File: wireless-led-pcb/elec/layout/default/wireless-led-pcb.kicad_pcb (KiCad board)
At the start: 2 copper layers, 225.7 x 100.8 mm, 0 parts

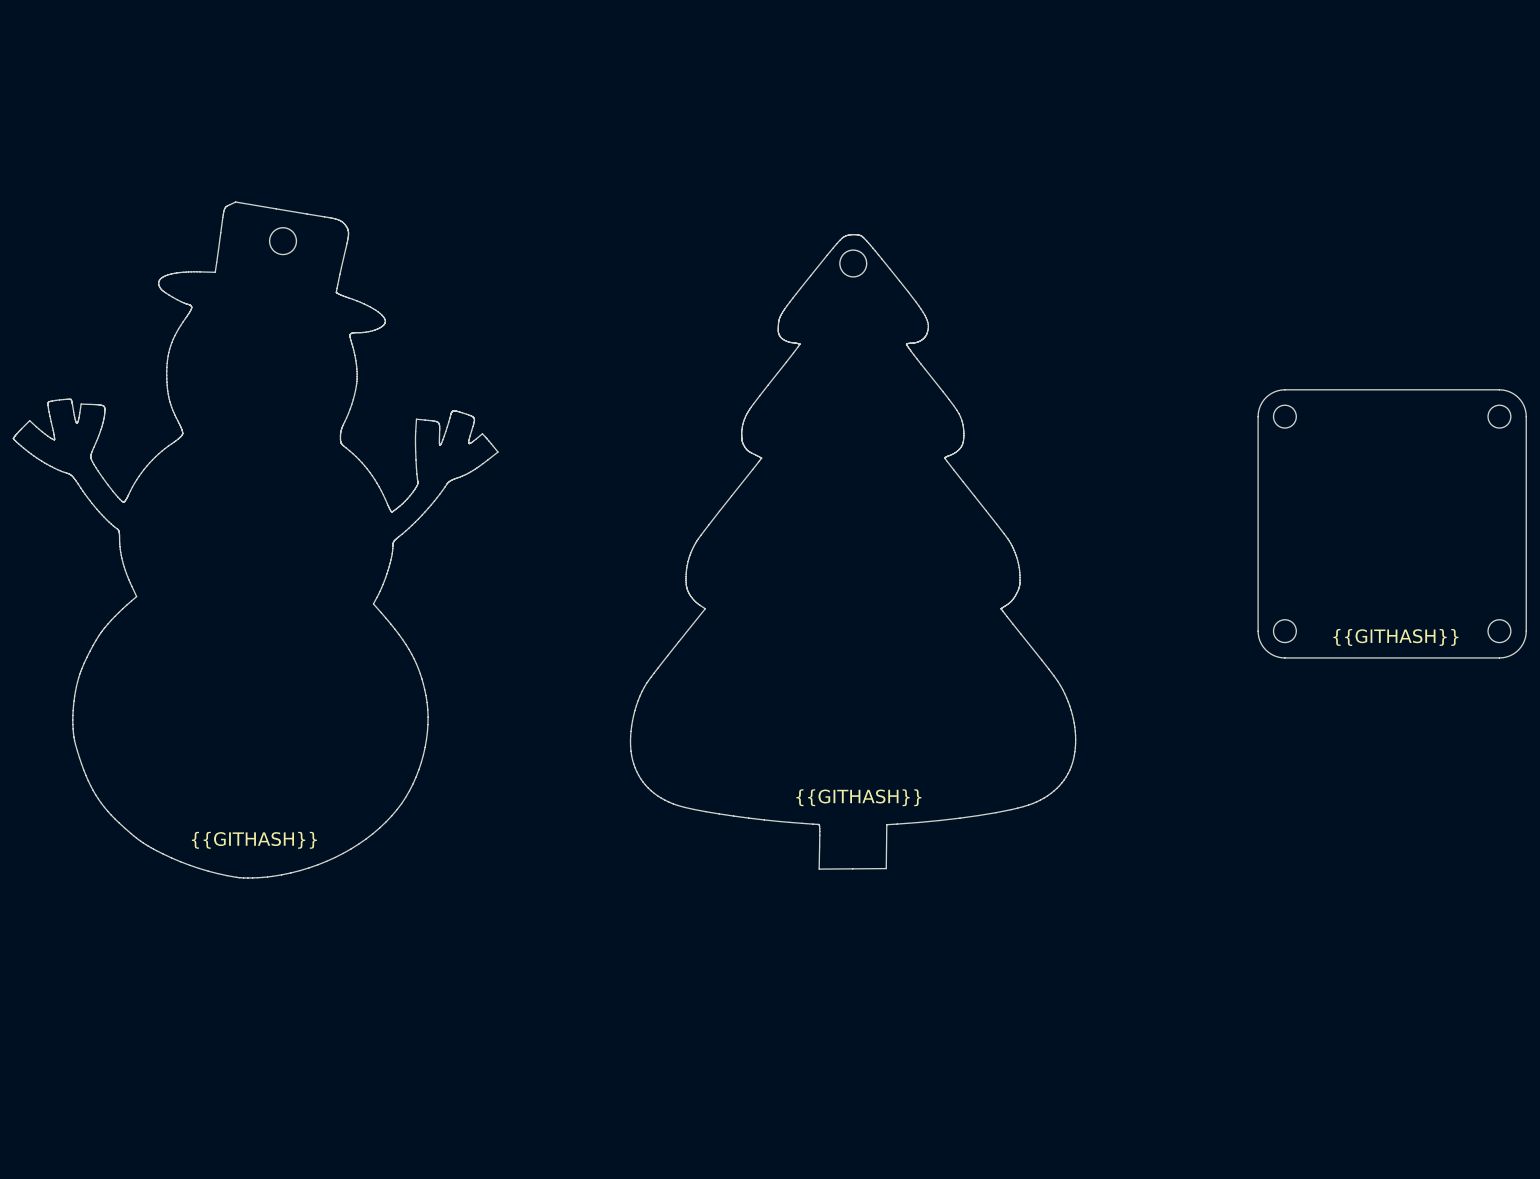
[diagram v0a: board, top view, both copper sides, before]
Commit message: Just started basic component organization in the layout. 1% done.
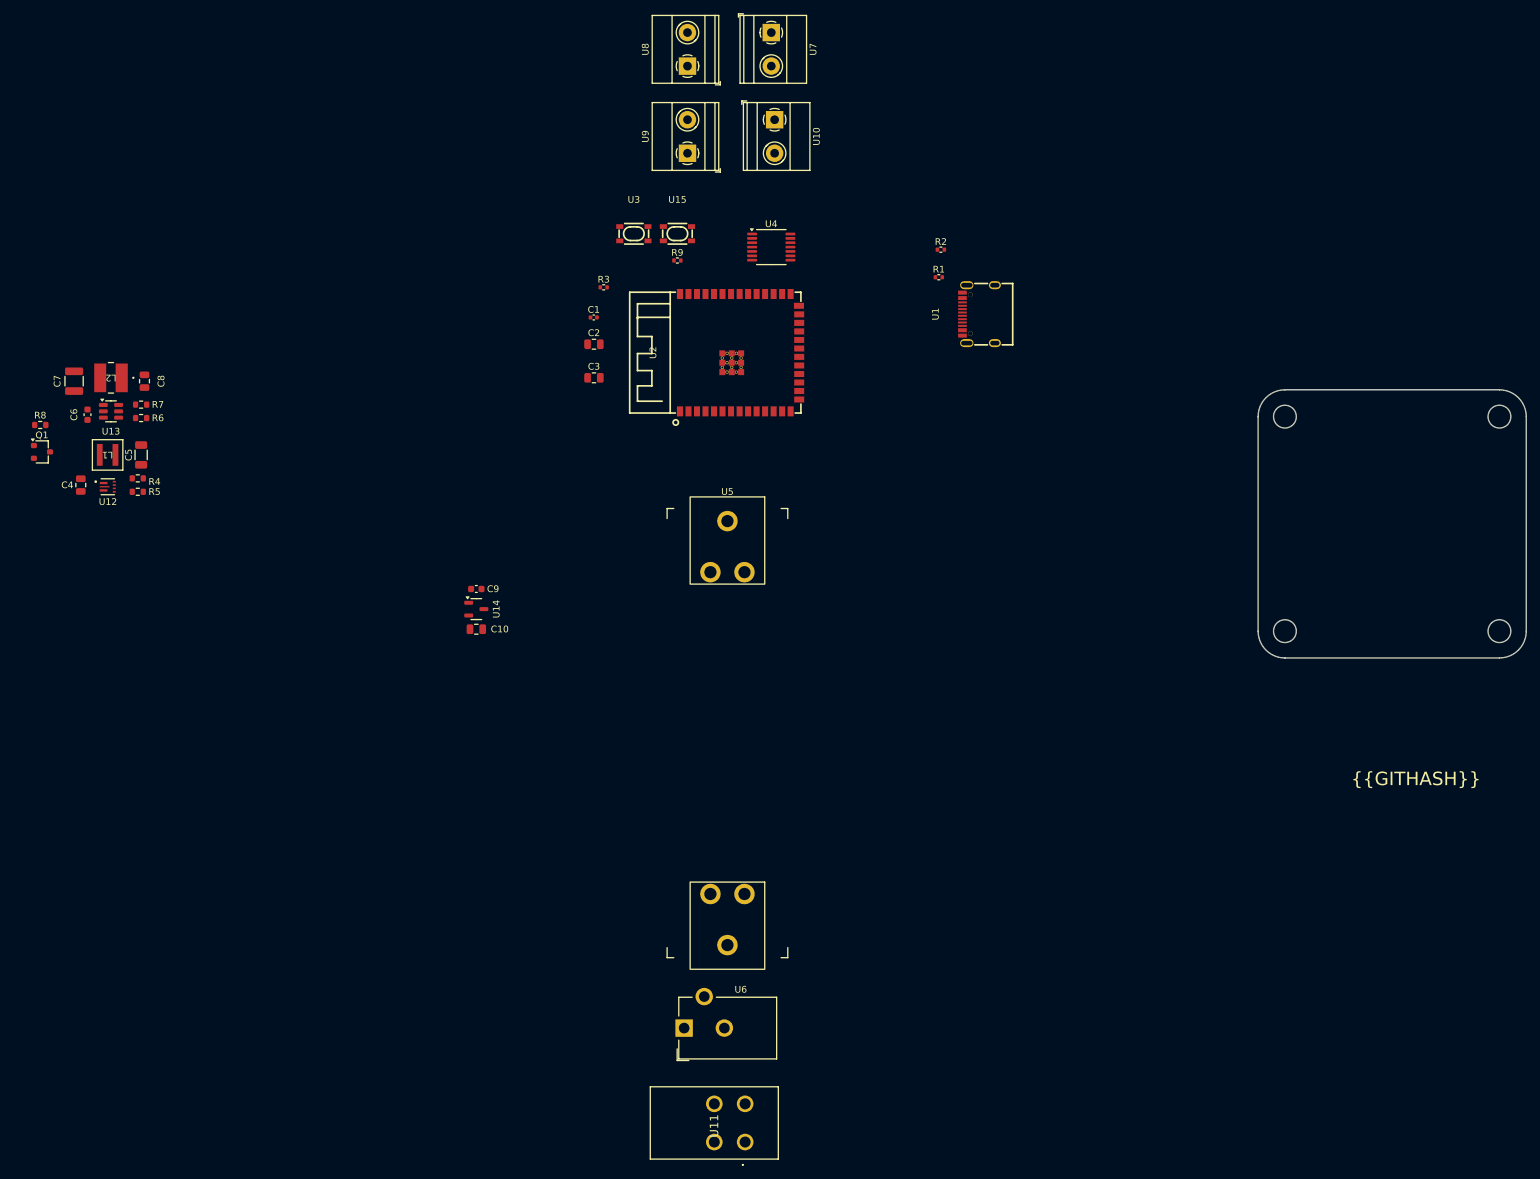
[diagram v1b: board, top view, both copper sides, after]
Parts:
- added C1: 16V 100nF X7R ±10% 0402 Multilayer Ceramic Capacitors MLCC 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, lib:C0402, F.Cu at (122.5, 67.0)
- added C10: 25V 10uF X5R ±10% 0805 Multilayer Ceramic Capacitors MLCC -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, lib:C0805, F.Cu at (105.0, 113.5)
- added C2: 25V 10uF X5R ±10% 0805 Multilayer Ceramic Capacitors MLCC -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, lib:C0805, F.Cu at (122.5, 71.0)
- added C3: 25V 10uF X5R ±10% 0805 Multilayer Ceramic Capacitors MLCC -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, lib:C0805, F.Cu at (122.5, 76.0)
- added C4: 25V 10uF X5R ±10% 0805 Multilayer Ceramic Capacitors MLCC -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, lib:C0805, F.Cu at (46.0, 92.0)
- added C5: 10V 47uF X5R ±20% 1206 Multilayer Ceramic Capacitors MLCC -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, lib:C1206, F.Cu at (55.0, 87.5)
- added C6: 10V 3.3uF X5R ±10% 0603 Multilayer Ceramic Capacitors MLCC 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, lib:C0603, F.Cu at (47.0, 81.5)
- added C7: 16V 47uF X7R ±10% 1210 Multilayer Ceramic Capacitors MLCC -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, lib:C1210, F.Cu at (45.0, 76.5)
- added C8: 50V 100nF X7R ±10% 0805 Multilayer Ceramic Capacitors MLCC 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, lib:C0805, F.Cu at (55.5, 76.5)
- added C9: 50V 1uF X5R ±10% 0603 Multilayer Ceramic Capacitors MLCC - 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, lib:C0603, F.Cu at (105.0, 107.5)
- added L1: 1uH +/- 20%, lib:IND_XAL4020_COC, F.Cu at (50.0, 87.5)
- added L2: 6.8uH +/- 20%, lib:IND_8357068_WRE, F.Cu at (50.5, 76.0)
- added Q1: , Package_TO_SOT_SMD:SC-59, F.Cu at (40.2, 87.0)
- added R1: 62.5mW Thick Film Resistors 50V ±100ppm/℃ ±1% 4.7kΩ 0402 Ch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, lib:R0402, F.Cu at (174.0, 61.0)
- added R2: 62.5mW Thick Film Resistors 50V ±100ppm/℃ ±1% 4.7kΩ 0402 Ch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, lib:R0402, F.Cu at (174.3, 56.9)
- added R3: 62.5mW Thick Film Resistors 50V ±100ppm/℃ ±1% 10kΩ 0402 Chi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, lib:R0402, F.Cu at (124.0, 62.5)
- added R4: 100mW Thick Film Resistors 75V ±100ppm/℃ ±1% 732kΩ 0603 Chi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, lib:R0603, F.Cu at (54.5, 91.0)
- added R5: 100mW Thick Film Resistors 75V ±100ppm/℃ ±1% 100kΩ 0603 Chi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, lib:R0603, F.Cu at (54.5, 93.0)
- added R6: 100mW Thick Film Resistors 75V ±100ppm/℃ ±1% 22kΩ 0603 Chip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, lib:R0603, F.Cu at (55.0, 82.0)
- added R7: 100mW Thick Film Resistors 75V ±100ppm/℃ ±1% 100kΩ 0603 Chi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, lib:R0603, F.Cu at (55.0, 80.0)
- added R8: 100mW Thick Film Resistors 75V ±100ppm/℃ ±1% 100kΩ 0603 Chi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, lib:R0603, F.Cu at (40.0, 83.0)
- added R9: 62.5mW Thick Film Resistors 50V ±100ppm/℃ ±1% 10kΩ 0402 Chi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, lib:R0402, F.Cu at (135.0, 58.5)
- added U1: , lib:USB-C-SMD_KH-TYPE-C-16P, F.Cu at (179.9, 66.5)
- added U10: , TerminalBlock_Phoenix:TerminalBlock_Phoenix_MKDS-1,5-2_1x02_P5.00mm_Horizontal, F.Cu at (149.5, 37.5)
- added U11: , lib:L201011MS02Q, F.Cu at (145.1, 190.0)
- added U12: , lib:CONV_TPS61022RWUR, F.Cu at (50.0, 92.2)
- added U13: , Package_TO_SOT_SMD:SOT-23-6, F.Cu at (50.5, 81.0)
- added U14: , Package_TO_SOT_SMD:SOT-23-3, F.Cu at (105.0, 110.5)
- added U15: , lib:KEY-SMD_4P-L4.2-W3.2-P2.20-LS4.6, F.Cu at (135.0, 54.5)
- added U2: , lib:WIRELM-SMD_ESP32-S3-WROOM-1, F.Cu at (144.3, 72.2)
- added U3: , lib:KEY-SMD_4P-L4.2-W3.2-P2.20-LS4.6, F.Cu at (128.5, 54.5)
- added U4: , Package_SO:TSSOP-14_4.4x5mm_P0.65mm, F.Cu at (149.0, 56.5)
- added U5: , lib:Battery-54, F.Cu at (142.5, 105.0)
- added U6: , Connector_BarrelJack:BarrelJack_CUI_PJ-102AH_Horizontal, F.Cu at (136.0, 173.0)
- added U7: , TerminalBlock_Phoenix:TerminalBlock_Phoenix_MKDS-1,5-2_1x02_P5.00mm_Horizontal, F.Cu at (149.0, 24.5)
- added U8: , TerminalBlock_Phoenix:TerminalBlock_Phoenix_MKDS-1,5-2_1x02_P5.00mm_Horizontal, F.Cu at (136.5, 29.5)
- added U9: , TerminalBlock_Phoenix:TerminalBlock_Phoenix_MKDS-1,5-2_1x02_P5.00mm_Horizontal, F.Cu at (136.5, 42.5)
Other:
- board size 225.7 x 100.8 mm -> 40 x 40 mm
